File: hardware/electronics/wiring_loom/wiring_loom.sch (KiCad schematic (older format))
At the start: 8 parts, among them J1 Conn_02x05_Top_Bottom, J2 Conn_02x15_Top_Bottom, J3 Conn_01x04, J4 Conn_01x04, J5 Conn_01x10, J6 Conn_01x16

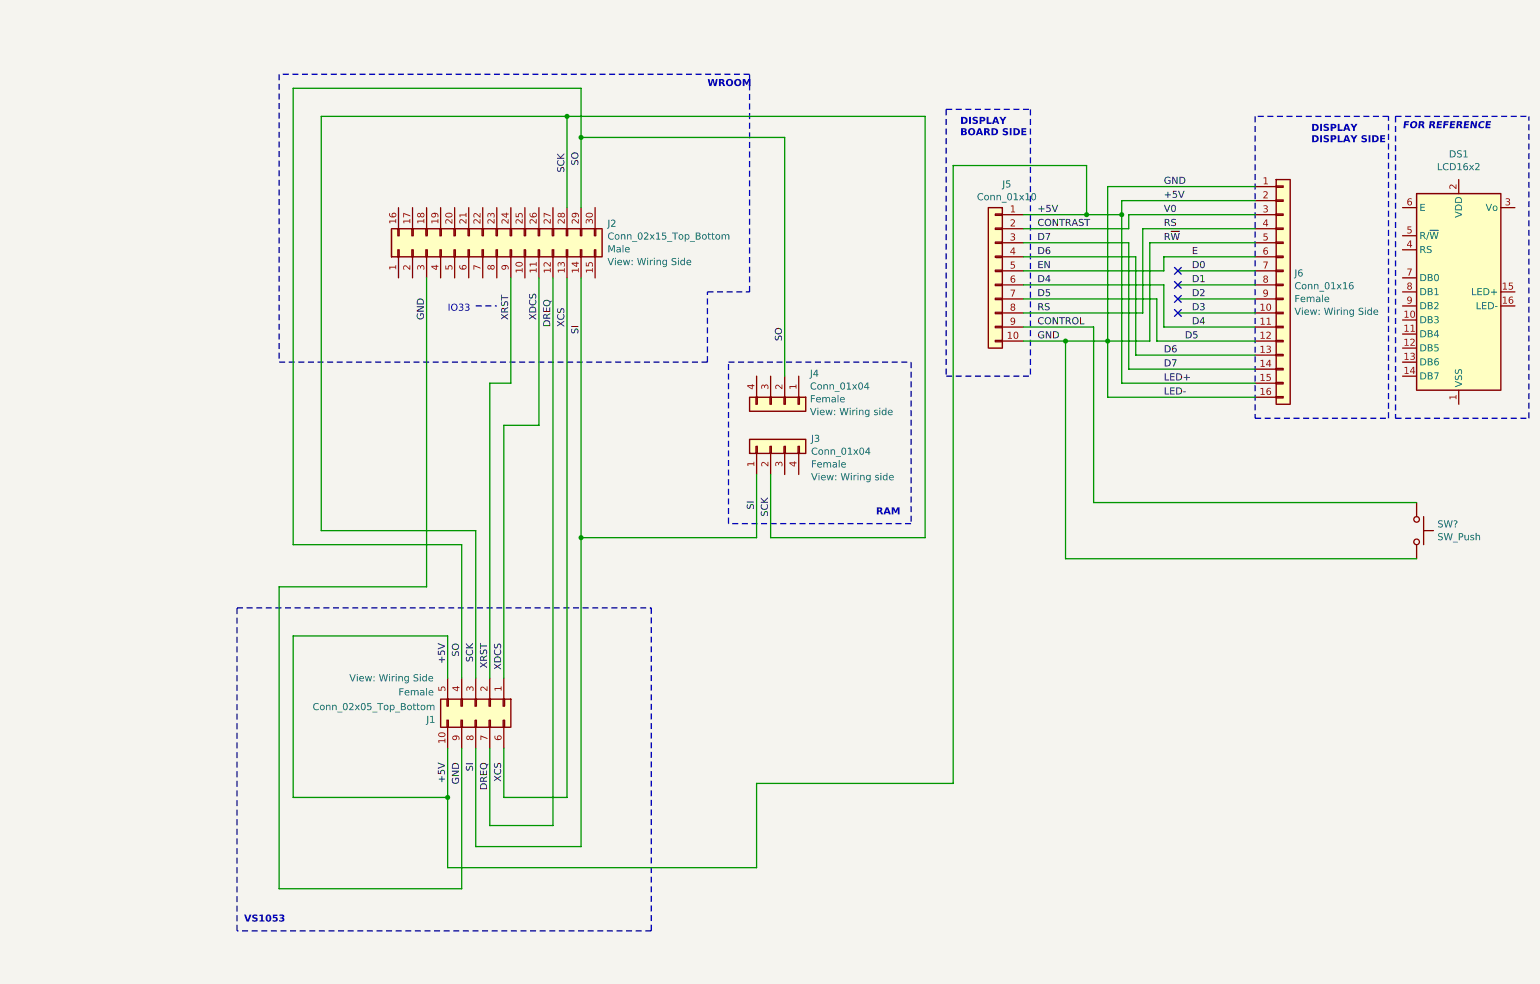
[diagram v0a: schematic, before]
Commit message: Updated the external wiring
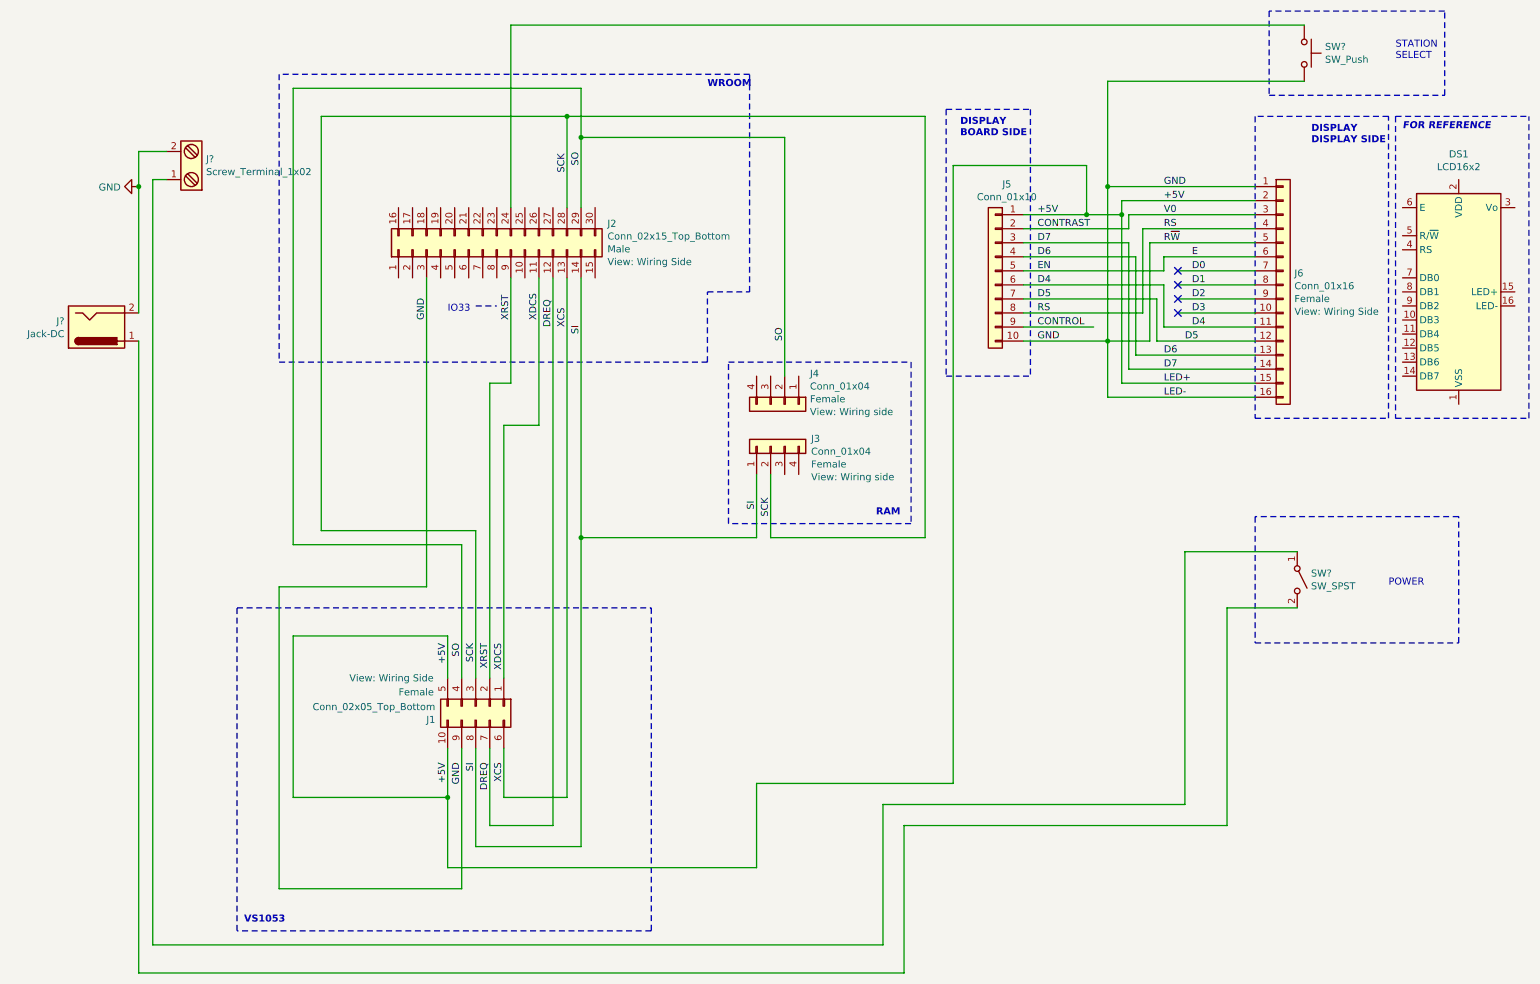
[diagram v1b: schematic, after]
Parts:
- removed SW?: SW_Push, symbol modular-internet-radio:SW_Push
- added J?: Screw_Terminal_1x02, symbol modular-internet-radio:Screw_Terminal_1x02
- added J?: Jack-DC, symbol modular-internet-radio:Jack-DC
- added SW?: SW_Push, symbol modular-internet-radio:SW_Push
- added SW?: SW_SPST, symbol modular-internet-radio:SW_SPST
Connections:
- net GND: now also J?.2, J?.2, SW?.2
- net at J2.24 (Pin_24): now also SW?.1
- new net: J?.1, SW?.1 (A)
- new net: J?.1, SW?.2 (B)
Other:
- note added: "POWER"
- note added: "STATION \nSELECT"
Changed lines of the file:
@@
 Text Label 8600 3350 0    50   ~ 0
 LED-
-$Comp
-L modular-internet-radio:SW_Push SW?
-U 1 1 5E7FA73C
-P 10400 4300
-F 0 "SW?" V 10354 4448 50  0000 L CNN
-F 1 "SW_Push" V 10445 4448 50  0000 L CNN
-F 2 "" H 10400 4500 50  0001 C CNN
-F 3 "" H 10400 4500 50  0001 C CNN
-	1    10400 4300
-	0    1    1    0
-$EndComp
 Text Label 7700 2050 0    50   ~ 0
 +5V
@@
 GND
 Wire Wire Line
-	8100 2850 8100 4100
-Wire Wire Line
-	8100 4100 10400 4100
-Wire Wire Line
 	7600 2850 8100 2850
 Wire Wire Line
-	10400 4500 7900 4500
-Wire Wire Line
-	7900 4500 7900 2950
-Wire Wire Line
-	7600 2950 7900 2950
-Wire Wire Line
 	8200 2950 8200 1850
 Wire Wire Line
 	8200 1850 9250 1850
-Wire Wire Line
-	7900 2950 8200 2950
-Connection ~ 7900 2950
 Wire Wire Line
 	8300 2050 8300 1950
@@
 Wire Wire Line
 	7100 6100 7100 1700
+$Comp
+L modular-internet-radio:SW_Push SW?
+U 1 1 5EA0B41B
+P 9600 900
+F 0 "SW?" V 9554 1048 50  0000 L CNN
+F 1 "SW_Push" V 9645 1048 50  0000 L CNN
+F 2 "" H 9600 1100 50  0001 C CNN
+F 3 "" H 9600 1100 50  0001 C CNN
+	1    9600 900
+	0    1    1    0
+$EndComp
+Wire Wire Line
+	3950 2000 3950 700
+Wire Wire Line
+	3950 700  9600 700
+Wire Wire Line
+	9600 1100 8200 1100
+Wire Wire Line
+	8200 1100 8200 1850
+Connection ~ 8200 1850
+$Comp
+L modular-internet-radio:Screw_Terminal_1x02 J?
+U 1 1 5EA12FAA
+P 1700 1700
+F 0 "J?" H 1620 1654 50  0000 R CNN
+F 1 "Screw_Terminal_1x02" H 1620 1745 50  0000 R CNN
+F 2 "" H 1700 1475 50  0001 C CNN
+F 3 "" H 1675 1700 50  0001 C CNN
+	1    1700 1700
+	-1   0    0    1
+$EndComp
+$Comp
+L modular-internet-radio:Jack-DC J?
+U 1 1 5EA1F24F
+P 1000 2850
+F 0 "J?" H 771 2808 50  0000 R CNN
+F 1 "Jack-DC" H 771 2899 50  0000 R CNN
+F 2 "" H 1050 2810 50  0001 C CNN
+F 3 "~" H 1050 2810 50  0001 C CNN
+	1    1000 2850
+	1    0    0    1
+$EndComp
+Wire Wire Line
+	1300 2750 1300 1850
+Wire Wire Line
+	1300 1600 1500 1600
+$Comp
+L modular-internet-radio:GND #PWR?
+U 1 1 5EA2E22E
+P 1300 1850
+F 0 "#PWR?" H 1300 1600 50  0001 C CNN
+F 1 "GND" V 1305 1722 50  0000 R CNN
+F 2 "" H 1300 1850 50  0000 C CNN
+F 3 "" H 1300 1850 50  0000 C CNN
+	1    1300 1850
+	0    1    1    0
+$EndComp
+Connection ~ 1300 1850
+Wire Wire Line
+	1300 1850 1300 1600
+$Comp
+L modular-internet-radio:SW_SPST SW?
+U 1 1 5EA3ADFF
+P 9550 4650
+F 0 "SW?" V 9504 4748 50  0000 L CNN
+F 1 "SW_SPST" V 9595 4748 50  0000 L CNN
+F 2 "" H 9550 4650 50  0001 C CNN
+F 3 "~" H 9550 4650 50  0001 C CNN
+	1    9550 4650
+	0    1    1    0
+$EndComp
+Wire Wire Line
+	7600 2950 8200 2950
+Wire Wire Line
+	1300 2950 1300 7450
+Wire Wire Line
+	1300 7450 6750 7450
+Wire Wire Line
+	6750 7450 6750 6400
+Wire Wire Line
+	6750 6400 9050 6400
+Wire Wire Line
+	9050 6400 9050 4850
+Wire Wire Line
+	9050 4850 9550 4850
+Wire Wire Line
+	9550 4450 8750 4450
+Wire Wire Line
+	8750 4450 8750 6250
+Wire Wire Line
+	8750 6250 6600 6250
+Wire Wire Line
+	6600 6250 6600 7250
+Wire Wire Line
+	6600 7250 1400 7250
+Wire Wire Line
+	1400 7250 1400 1800
+Wire Wire Line
+	1400 1800 1500 1800
+Text Notes 10250 950  0    50   ~ 0
+STATION \nSELECT
+Wire Notes Line
+	9350 600  9350 1200
+Wire Notes Line
+	9350 1200 10600 1200
+Wire Notes Line
+	10600 1200 10600 600
+Wire Notes Line
+	10600 600  9350 600
+Text Notes 10200 4700 0    50   ~ 0
+POWER
+Wire Notes Line
+	9250 5100 10700 5100
+Wire Notes Line
+	10700 5100 10700 4200
+Wire Notes Line
+	10700 4200 9250 4200
+Wire Notes Line
+	9250 4200 9250 5100
 $EndSCHEMATC
